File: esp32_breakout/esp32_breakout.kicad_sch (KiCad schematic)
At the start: 25 parts, among them J1 JST B5B-PH-K-S, J10 JST B6B-PH-K-S, J2 JST B5B-PH-K-S, J3 JST B7B-PH-K-S, J4 XT30U-M, J5 HDR M VERT 12p 2.54mm, J9 JST B6B-PH-K-S, SW1 SS12D10, U1 ESP32 DEV KIT Module 30-pin, U2 LM2596 Module

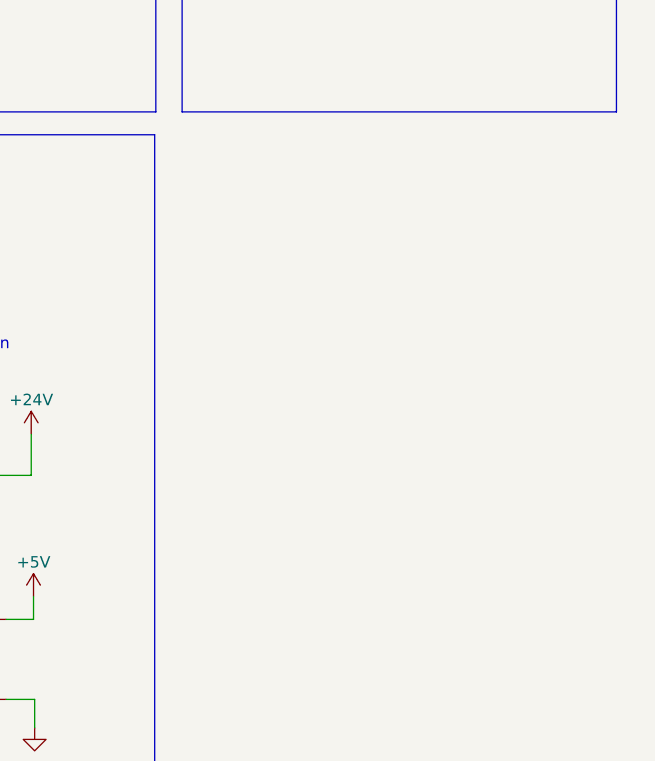
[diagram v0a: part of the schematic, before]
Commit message: Started lds_breakout
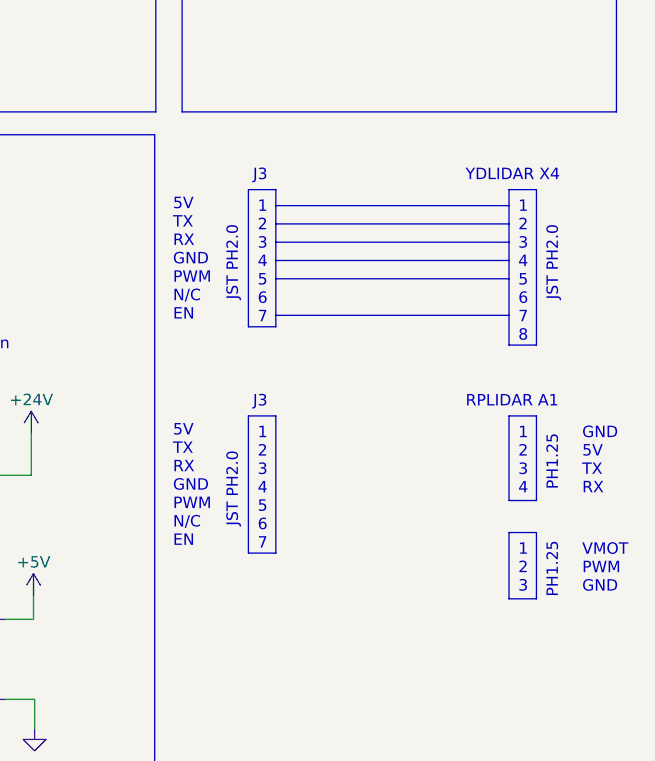
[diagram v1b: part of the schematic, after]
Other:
- note added: "5V TX RX GND PWM N/C EN"
- note added: "GND 5V TX RX"
- note added: "J3"
- note added: "JST PH2.0"
- note added: "PH1.25"
- note added: "RPLIDAR A1"
- note added: "VMOT PWM GND"
- note added: "YDLIDAR X4"
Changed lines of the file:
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@@
+    (stroke (width 0) (type default))
+  )
+  (polyline (pts (xy 226.314 109.22) (xy 252.222 109.22))
+    (stroke (width 0) (type default))
+  )
+  (polyline (pts (xy 226.314 103.124) (xy 252.222 103.124))
     (stroke (width 0) (type default))
   )
@@
     (stroke (width 0) (type default))
   )
+  (polyline (pts (xy 226.314 115.316) (xy 252.222 115.316))
+    (stroke (width 0) (type default))
+  )
   (wire (pts (xy 168.148 61.214) (xy 187.96 61.214))
     (stroke (width 0) (type default))
@@
     (stroke (width 0) (type default))
   )
+  (polyline (pts (xy 226.314 111.252) (xy 252.222 111.252))
+    (stroke (width 0) (type default))
+  )
   (wire (pts (xy 142.748 49.53) (xy 159.258 49.53))
     (stroke (width 0) (type default))
@@
     (stroke (width 0) (type default))
   )
+  (polyline (pts (xy 226.314 105.156) (xy 252.222 105.156))
+    (stroke (width 0) (type default))
+  )
   (wire (pts (xy 14.605 41.91) (xy 33.528 41.91))
     (stroke (width 0) (type default))
@@
     (stroke (width 0) (type default))
   )
+  (polyline (pts (xy 226.314 107.188) (xy 252.222 107.188))
+    (stroke (width 0) (type default))
+  )
   (polyline (pts (xy 197.612 65.024) (xy 202.184 65.024))
     (stroke (width 0) (type default))
@@
     (fill (type none))
   )
+  (text_box "1\n2\n3\n4"
+    (at 252.222 126.492 0) (size 3.048 9.398)
+    (stroke (width 0) (type default))
+    (fill (type none))
+    (effects (font (size 1.27 1.27)) (justify left top))
+  )
+  (text_box "1\n2\n3\n4\n5\n6\n7\n8"
+    (at 252.222 101.346 0) (size 3.048 17.272)
+    (stroke (width 0) (type default))
+    (fill (type none))
+    (effects (font (size 1.27 1.27)) (justify left top))
+  )
+  (text_box "1\n2\n3\n4\n5\n6\n7"
+    (at 223.266 101.346 0) (size 3.048 15.24)
+    (stroke (width 0) (type default))
+    (fill (type none))
+    (effects (font (size 1.27 1.27)) (justify left top))
+  )
+  (text_box "1\n2\n3"
+    (at 252.222 139.446 0) (size 3.048 7.366)
+    (stroke (width 0) (type default))
+    (fill (type none))
+    (effects (font (size 1.27 1.27)) (justify left top))
+  )
+  (text_box "1\n2\n3\n4\n5\n6\n7"
+    (at 223.266 126.492 0) (size 3.048 15.24)
+    (stroke (width 0) (type default))
+    (fill (type none))
+    (effects (font (size 1.27 1.27)) (justify left top))
+  )
   (text "SONAR\nUS-100" (at 201.422 44.958 90)
     (effects (font (size 1.27 1.27)) (justify left bottom))
   )
+  (text "J3" (at 223.774 125.73 0)
+    (effects (font (size 1.27 1.27)) (justify left bottom))
+  )
   (text "GND\nGND\nEcho/Rx\nTrig/Tx\nVCC 5V" (at 203.2 45.974 0)
     (effects (font (size 1.27 1.27)) (justify left bottom))
   )
   (text "SPARE GPIO" (at 200.152 62.23 90)
+    (effects (font (size 1.27 1.27)) (justify left bottom))
+  )
+  (text "VMOT\nPWM\nGND" (at 260.35 146.304 0)
+    (effects (font (size 1.27 1.27)) (justify left bottom))
+  )
+  (text "JST PH2.0" (at 222.25 113.792 90)
+    (effects (font (size 1.27 1.27)) (justify left bottom))
+  )
+  (text "5V\nTX\nRX\nGND\nPWM\nN/C\nEN" (at 214.884 116.078 0)
     (effects (font (size 1.27 1.27)) (justify left bottom))
   )
@@
     (effects (font (size 1.27 1.27)) (justify left bottom))
   )
+  (text "YDLIDAR X4" (at 247.396 100.584 0)
+    (effects (font (size 1.27 1.27)) (justify left bottom))
+  )
   (text "BATTERY\nInput voltage 24V\nMax 24V input current approx. 2.2A with both motors stalled\n\nSafety\n- 24V input/output overcurrent protection using a fuse\n  Use a slow-blow fuse to prevent inrush current tripping the fuse\n- 24V input reverse polarity protection using a Schottki diode\n- input overvoltage LM2596 40V max; motors not protected\n- 5V output LM2596 provides current limit, short, thermal protection\nWARNING: do NOT short 24V with any 5V or 3.3V signals"
     (at 137.16 121.412 0)
     (effects (font (size 1.27 1.27)) (justify left bottom))
   )
+  (text "JST PH2.0" (at 257.81 113.792 90)
+    (effects (font (size 1.27 1.27)) (justify left bottom))
+  )
+  (text "J3" (at 223.774 100.584 0)
+    (effects (font (size 1.27 1.27)) (justify left bottom))
+  )
   (text "MOTORS\n\nCHR-GM25-BLDC2418 i45\nType BLDC\nVoltage 24V, I/O 5V\nDiameter 25mm, weight 69g\nMax RPM 200, rated RPM 145\nRated torque 1.5Kg*cm, stall torque 5Kg*cm\nMax power 2.5W, stall current 0.65A\nhttps://www.aliexpress.us/item/2251832633601682.html"
     (at 17.272 118.11 0)
     (effects (font (size 1.27 1.27)) (justify left bottom))
   )
+  (text "GND\n5V\nTX\nRX" (at 260.35 135.382 0)
+    (effects (font (size 1.27 1.27)) (justify left bottom))
+  )
+  (text "RPLIDAR A1" (at 247.396 125.73 0)
+    (effects (font (size 1.27 1.27)) (justify left bottom))
+  )
+  (text "PH1.25" (at 257.81 146.812 90)
+    (effects (font (size 1.27 1.27)) (justify left bottom))
+  )
+  (text "5V\nTX\nRX\nGND\nPWM\nN/C\nEN" (at 214.884 141.224 0)
+    (effects (font (size 1.27 1.27)) (justify left bottom))
+  )
+  (text "JST PH2.0" (at 222.25 138.938 90)
+    (effects (font (size 1.27 1.27)) (justify left bottom))
+  )
   (text "LASER DISTANCE SENSOR\n\nYDLidar X4, https://www.ydlidar.com/\nYDLidar X4 connector pinout:\nVCC 5V\nTX all I/O 3.3V\nRX\nGND\nM_SCTR speed\nDEV_EN N/C\nM_EN\nN/C"
     (at 82.042 124.46 0)
     (effects (font (size 1.27 1.27)) (justify left bottom))
   )
+  (text "PH1.25" (at 257.81 134.874 90)
+    (effects (font (size 1.27 1.27)) (justify left bottom))
+  )
